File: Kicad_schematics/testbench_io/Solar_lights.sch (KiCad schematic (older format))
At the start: 13 parts, among them J301 Conn_01x12, Q301 IPD50R380CE, Q302 IPD50R380CE, Q303 IPD50R380CE, Q304 IPD50R380CE, Q305 IPD50R380CE, Q306 IPD50R380CE

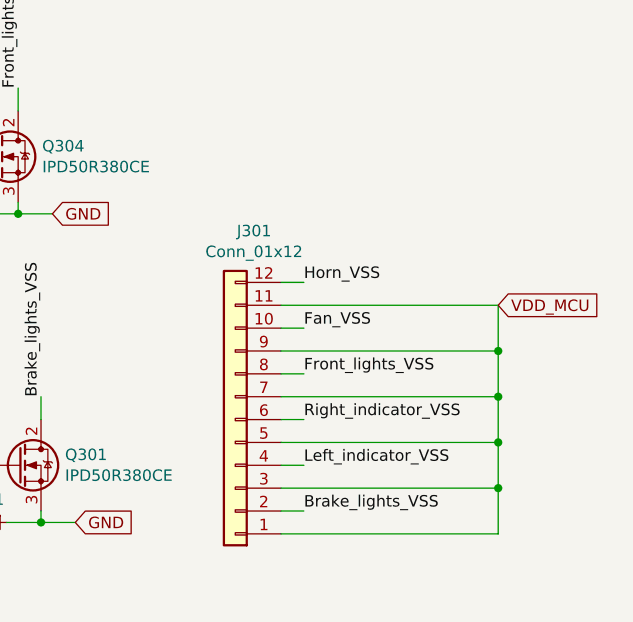
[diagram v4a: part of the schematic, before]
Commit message: Change of connector
Changed a connector that wasn't available
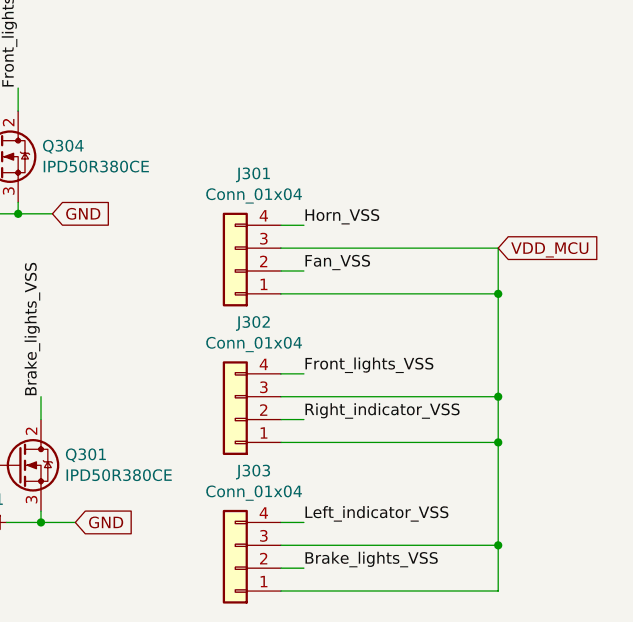
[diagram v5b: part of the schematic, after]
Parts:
- removed J301: Conn_01x12, Connector_JST:JST_XH_S12B-XH-A-1_1x12_P2.50mm_Horizontal, symbol Connector_Generic:Conn_01x12
- added J301, J302, J303: Conn_01x04, Connector_JST:JST_XH_S4B-XH-A_1x04_P2.50mm_Horizontal, symbol Connector_Generic:Conn_01x04
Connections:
- net Brake_lights_VSS: now also J303.2 (Pin_2)
- net Fan_VSS: now also J301.2 (Pin_2)
- net Front_lights_VSS: now also J302.4 (Pin_4)
- net Horn_VSS: now also J301.4 (Pin_4)
- net Left_indicator_VSS: now also J303.4 (Pin_4)
- net Right_indicator_VSS: now also J302.2 (Pin_2)
- net VDD_MCU: now also J301.1 (Pin_1), J301.3 (Pin_3), J302.1 (Pin_1), J302.3 (Pin_3), J303.1 (Pin_1), J303.3 (Pin_3)
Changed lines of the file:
@@
 Text HLabel 5200 3400 1    50   Input ~ 0
 Front_acti
-Text Label 6800 4950 0    50   ~ 0
+Text Label 6800 5200 0    50   ~ 0
 Brake_lights_VSS
-Text Label 6800 4750 0    50   ~ 0
+Text Label 6800 5000 0    50   ~ 0
 Left_indicator_VSS
 Text Label 6800 4550 0    50   ~ 0
@@
 	1    0    0    -1
 $EndComp
-Text GLabel 7650 4050 2    50   Input ~ 0
+Text GLabel 7650 3800 2    50   Input ~ 0
 VDD_MCU
 Wire Wire Line
-	6700 4750 6800 4750
-Wire Wire Line
-	6700 4950 6800 4950
+	6700 5000 6800 5000
+Wire Wire Line
+	6700 5200 6800 5200
 Wire Wire Line
 	7650 4450 7650 4650
@@
 Connection ~ 7650 4650
 Wire Wire Line
-	6700 4850 7650 4850
-Wire Wire Line
-	7650 4650 7650 4850
-Wire Wire Line
-	7650 4850 7650 5050
-Wire Wire Line
-	6700 5050 7650 5050
-Connection ~ 7650 4850
+	6700 5100 7650 5100
+Wire Wire Line
+	7650 4650 7650 5100
+Wire Wire Line
+	7650 5100 7650 5300
+Wire Wire Line
+	6700 5300 7650 5300
+Connection ~ 7650 5100
 Wire Wire Line
 	4800 4550 4800 4450
@@
 Fan_acti
 Wire Wire Line
-	7650 4250 7650 4450
-Connection ~ 7650 4450
+	7650 4000 7650 4450
 Text Label 4800 4450 1    50   ~ 0
 Fan_VSS
 Wire Wire Line
 	6700 4450 7650 4450
-Text Label 6800 4150 0    50   ~ 0
+Text Label 6800 3900 0    50   ~ 0
 Fan_VSS
 Wire Wire Line
-	6800 4150 6700 4150
-Wire Wire Line
-	6700 4250 7650 4250
+	6800 3900 6700 3900
+Wire Wire Line
+	6700 4000 7650 4000
 Wire Wire Line
 	3900 4600 3900 4500
@@
 Text Label 3900 4500 1    50   ~ 0
 Horn_VSS
-$Comp
-L Connector_Generic:Conn_01x12 J301
-U 1 1 603A60EB
+Text Label 6800 3700 0    50   ~ 0
+Horn_VSS
+Wire Wire Line
+	6700 3800 7650 3800
+Wire Wire Line
+	7650 3800 7650 4000
+Connection ~ 7650 4000
+Wire Wire Line
+	6800 3700 6700 3700
+$Comp
+L Connector_Generic:Conn_01x04 J301
+U 1 1 6019E71D
+P 6500 3900
+F 0 "J301" H 6418 3475 50  0000 C CNN
+F 1 "Conn_01x04" H 6418 3566 50  0000 C CNN
+F 2 "Connector_JST:JST_XH_S4B-XH-A_1x04_P2.50mm_Horizontal" H 6500 3900 50  0001 C CNN
+F 3 "~" H 6500 3900 50  0001 C CNN
+	1    6500 3900
+	-1   0    0    1
+$EndComp
+Connection ~ 7650 4450
+$Comp
+L Connector_Generic:Conn_01x04 J302
+U 1 1 601C60D2
 P 6500 4550
-F 0 "J301" H 6418 3725 50  0000 C CNN
-F 1 "Conn_01x12" H 6418 3816 50  0000 C CNN
-F 2 "Connector_JST:JST_XH_S12B-XH-A-1_1x12_P2.50mm_Horizontal" H 6500 4550 50  0001 C CNN
+F 0 "J302" H 6418 4125 50  0000 C CNN
+F 1 "Conn_01x04" H 6418 4216 50  0000 C CNN
+F 2 "Connector_JST:JST_XH_S4B-XH-A_1x04_P2.50mm_Horizontal" H 6500 4550 50  0001 C CNN
 F 3 "~" H 6500 4550 50  0001 C CNN
 	1    6500 4550
 	-1   0    0    1
 $EndComp
-Text Label 6800 3950 0    50   ~ 0
-Horn_VSS
-Wire Wire Line
-	6700 4050 7650 4050
-Wire Wire Line
-	7650 4050 7650 4250
-Connection ~ 7650 4250
-Wire Wire Line
-	6800 3950 6700 3950
+$Comp
+L Connector_Generic:Conn_01x04 J303
+U 1 1 601C67E7
+P 6500 5200
+F 0 "J303" H 6418 4775 50  0000 C CNN
+F 1 "Conn_01x04" H 6418 4866 50  0000 C CNN
+F 2 "Connector_JST:JST_XH_S4B-XH-A_1x04_P2.50mm_Horizontal" H 6500 5200 50  0001 C CNN
+F 3 "~" H 6500 5200 50  0001 C CNN
+	1    6500 5200
+	-1   0    0    1
+$EndComp
 $EndSCHEMATC
